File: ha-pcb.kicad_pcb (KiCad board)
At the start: 2 copper layers, 137.2 x 110.7 mm, 55 parts, among them J1 RJ45_NC1W, J10 RJ45_1W1W, J11 RJ45_1W1W, J12 3.5Inch_Audio, J13 3.5Inch_Audio, J14 3.5Inch_Audio, J15 3.5Inch_Audio, J16 3.5Inch_Audio, J17 locked, J2 12V IN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

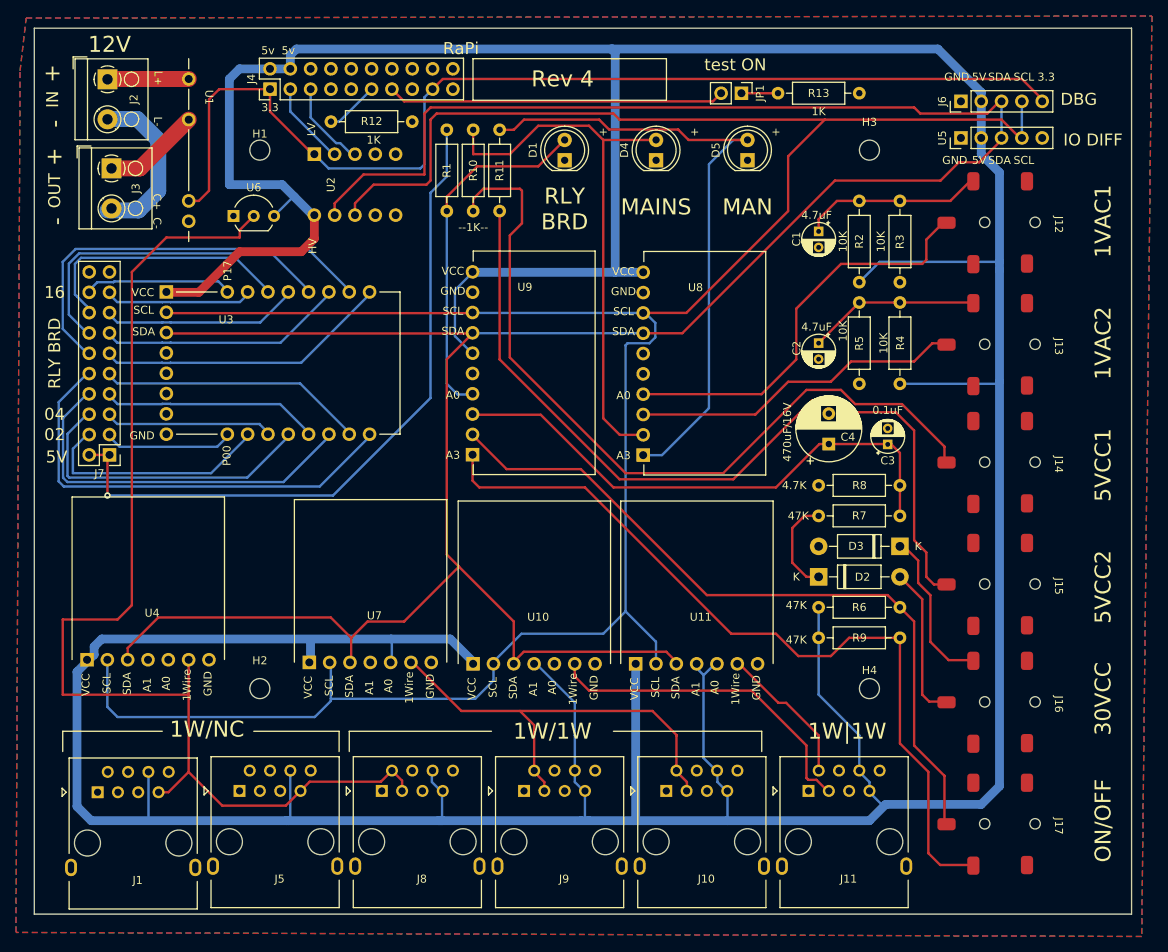
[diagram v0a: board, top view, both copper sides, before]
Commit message: Sent pcb to manufacturer step 1
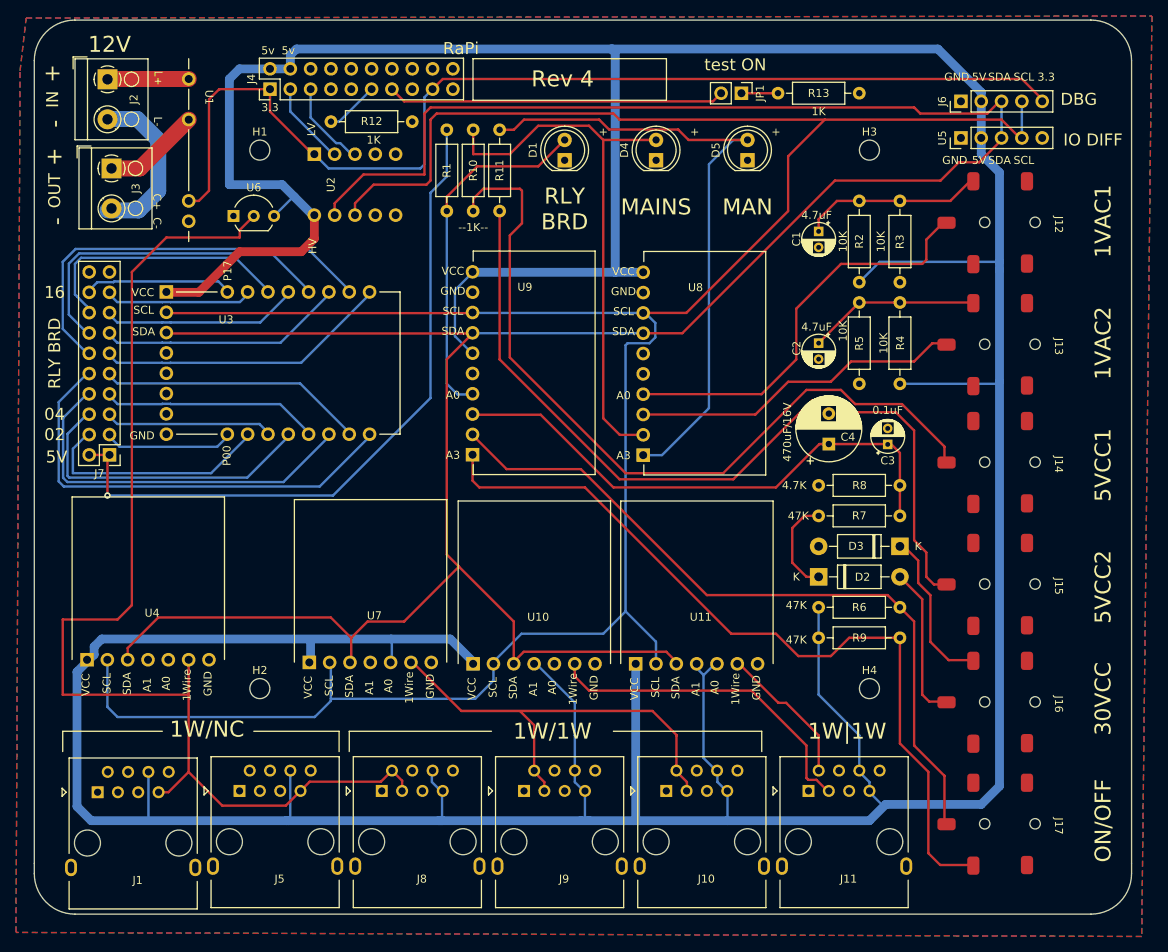
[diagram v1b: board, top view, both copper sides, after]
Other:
- board size 137.2 x 110.7 mm -> 137.2 x 111.8 mm
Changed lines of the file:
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@@
     (property "Sheetname" "")
     (attr exclude_from_pos_files)
-    (fp_text reference "H2" (at 0 -3.5) (layer "F.SilkS")
+    (fp_text reference "H2" (at 0 -2.286) (layer "F.SilkS")
       (effects (font (size 1 1) (thickness 0.15)))
     )
@@
     (property "Sheetname" "")
     (attr exclude_from_pos_files)
-    (fp_text reference "H3" (at 0 -3.5) (layer "F.SilkS")
+    (fp_text reference "H3" (at 0 -2.286) (layer "F.SilkS")
       (effects (font (size 1 1) (thickness 0.15)))
     )
@@
     (property "Sheetname" "")
     (attr exclude_from_pos_files)
-    (fp_text reference "H1" (at 0 -2.032) (layer "F.SilkS")
+    (fp_text reference "H1" (at 0 -2.286) (layer "F.SilkS")
       (effects (font (size 1 1) (thickness 0.15)))
     )
@@
   (gr_line (start 113.03 119.38) (end 131.572 119.38) (layer "F.SilkS") (width 0.153))
   (gr_line (start 44.196 119.38) (end 56.642 119.38) (layer "F.SilkS") (width 0.153))
-  (gr_rect (start 40.64 31.496) (end 177.8 142.24) (layer "Edge.Cuts") (width 0.1) (fill none))
+  (gr_arc (start 177.8 137.16) (mid 176.312102 140.752102) (end 172.72 142.24) (layer "Edge.Cuts") (width 0.1))
+  (gr_line (start 177.8 137.16) (end 177.8 135.89) (layer "Edge.Cuts") (width 0.1))
+  (gr_arc (start 45.72 142.24) (mid 42.127898 140.752102) (end 40.64 137.16) (layer "Edge.Cuts") (width 0.1))
+  (gr_line (start 40.64 35.56) (end 40.640004 135.89) (layer "Edge.Cuts") (width 0.1))
+  (gr_arc (start 40.639996 35.56) (mid 42.127894 31.967898) (end 45.719996 30.48) (layer "Edge.Cuts") (width 0.1))
+  (gr_line (start 172.72 30.479996) (end 45.719996 30.48) (layer "Edge.Cuts") (width 0.1))
+  (gr_arc (start 172.72 30.479996) (mid 176.312102 31.967894) (end 177.8 35.559996) (layer "Edge.Cuts") (width 0.1))
+  (gr_line (start 177.8 135.89) (end 177.8 35.559996) (layer "Edge.Cuts") (width 0.1))
+  (gr_line (start 45.72 142.24) (end 172.72 142.24) (layer "Edge.Cuts") (width 0.1))
+  (gr_line (start 40.640004 135.89) (end 40.64 137.16) (layer "Edge.Cuts") (width 0.1))
   (gr_line (start 68.834 114.046) (end 184.404 114.046) (layer "User.1") (width 0.15))
   (gr_line (start 68.834 46.736) (end 184.404 46.736) (layer "User.1") (width 0.15))
